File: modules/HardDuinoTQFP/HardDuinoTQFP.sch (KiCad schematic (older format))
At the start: 6 parts, among them J1 Conn_01x10_Male, J2 Conn_01x10_Male

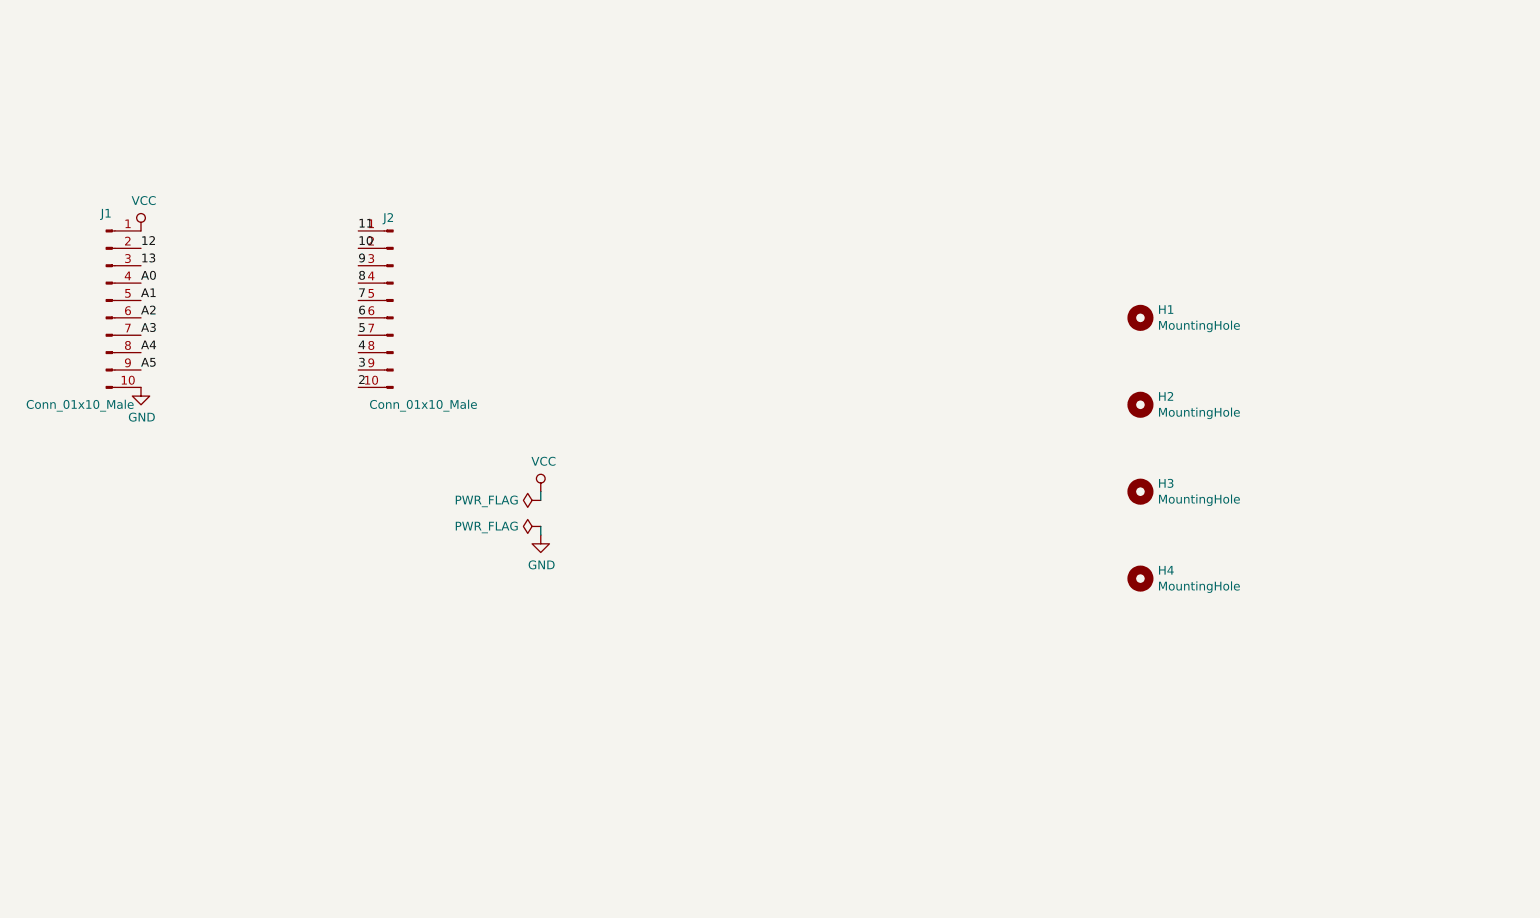
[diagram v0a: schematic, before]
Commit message: HardDuino TQFP is ready
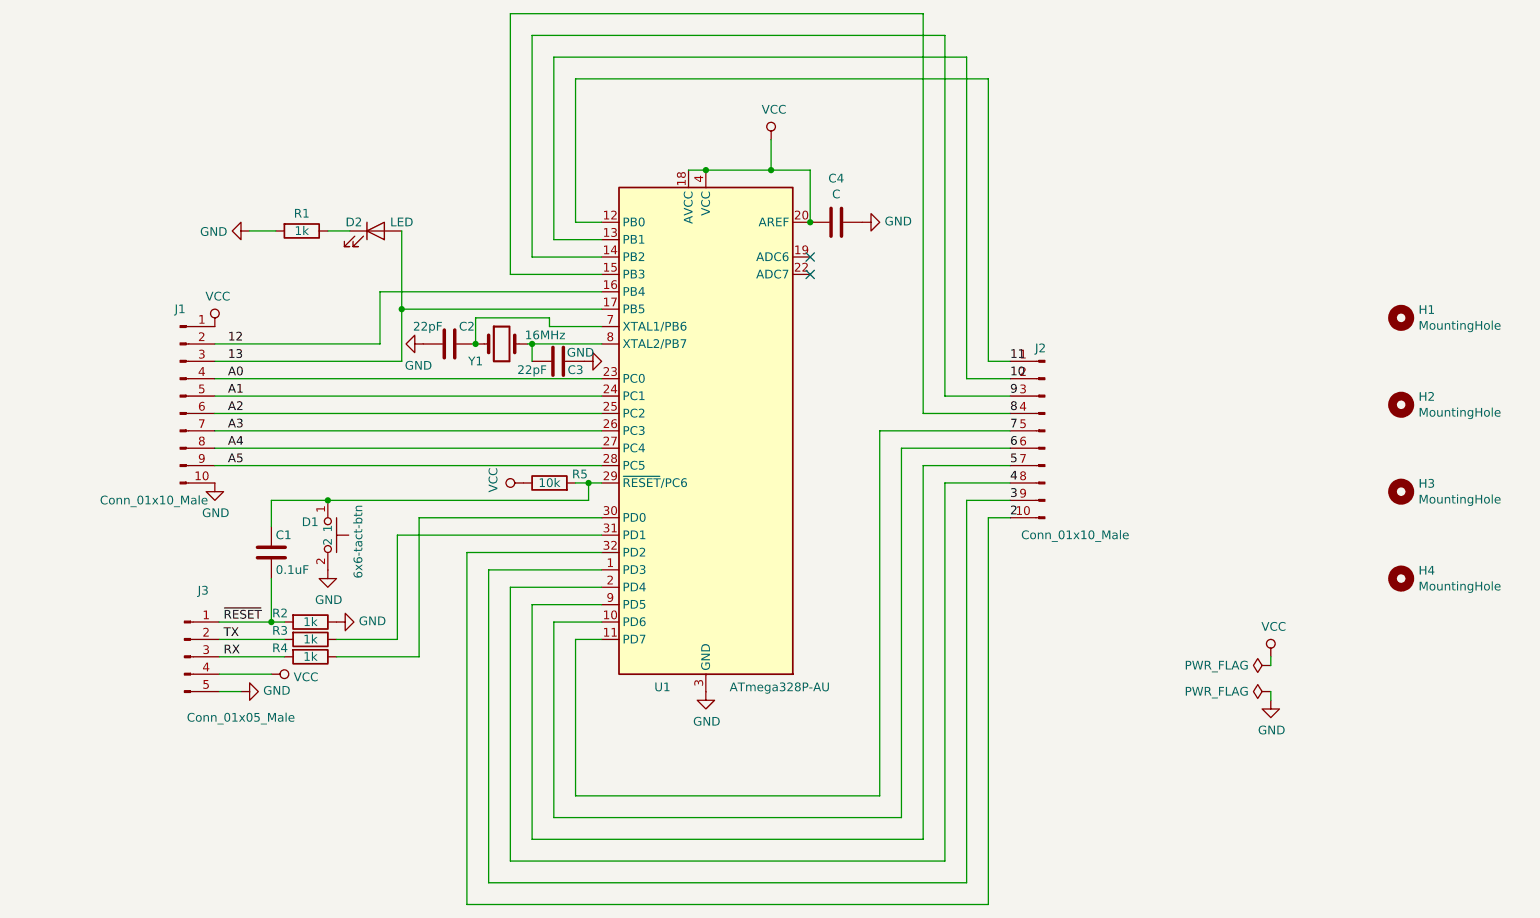
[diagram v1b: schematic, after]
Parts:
- added C1: 0.1uF, Capacitor_SMD:C_0805_2012Metric_Pad1.15x1.40mm_HandSolder, symbol Device:C
- added C2, C3: 22pF, Capacitor_SMD:C_0805_2012Metric_Pad1.15x1.40mm_HandSolder, symbol Device:C
- added C4: C, Capacitor_SMD:C_0805_2012Metric_Pad1.15x1.40mm_HandSolder, symbol Device:C
- added D1: 6x6-tact-btn, CommonLibrary:6x6-tact-btn, symbol CommonLibrary:6x6-tact-btn
- added D2: LED, LED_SMD:LED_0805_2012Metric_Pad1.15x1.40mm_HandSolder, symbol Device:LED
- added J3: Conn_01x05_Male, Connector_PinHeader_2.54mm:PinHeader_1x05_P2.54mm_Vertical, symbol Connector:Conn_01x05_Male
- added R1, R2, R3, R4: 1k, Resistor_SMD:R_0805_2012Metric_Pad1.15x1.40mm_HandSolder, symbol Device:R
- added R5: 10k, Resistor_SMD:R_0805_2012Metric_Pad1.15x1.40mm_HandSolder, symbol Device:R
- added U1: ATmega328P-AU, Package_QFP:TQFP-32_7x7mm_P0.8mm, symbol MCU_Microchip_ATmega:ATmega328P-AU
- added Y1: 16MHz, Crystal:Crystal_HC49-U_Vertical, symbol Device:Crystal
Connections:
- net 10: now also U1.13 (PB1)
- net 11: now also U1.12 (PB0)
- net 12: now also U1.16 (PB4)
- net 13: now also D2.2 (A), U1.17 (PB5)
- net 2: now also U1.32 (PD2)
- net 3: now also U1.1 (PD3)
- net 4: now also U1.2 (PD4)
- net 5: now also U1.9 (PD5)
- net 6: now also U1.10 (PD6)
- net 7: now also U1.11 (PD7)
- net 8: now also U1.15 (PB3)
- net 9: now also U1.14 (PB2)
- net A0: now also U1.23 (PC0)
- net A1: now also U1.24 (PC1)
- net A2: now also U1.25 (PC2)
- net A3: now also U1.26 (PC3)
- net A4: now also U1.27 (PC4)
- net A5: now also U1.28 (PC5)
- net GND: now also C2.2, C3.1, C4.1, D1.2, J3.5 (Pin_5), R1.2, R2.1, U1.21 (GND), U1.3 (GND), U1.5 (GND)
- net VCC: now also C4.2, J3.4 (Pin_4), R5.1, U1.18 (AVCC), U1.20 (AREF), U1.4 (VCC), U1.6 (VCC)
- new net: C1.1, D1.1, R5.2, U1.29 (~RESET~/PC6)
- new net: R4.1, U1.30 (PD0)
- new net: R3.1, U1.31 (PD1)
- new net: C2.1, U1.7 (XTAL1/PB6), Y1.1
- new net: C3.2, U1.8 (XTAL2/PB7), Y1.2
- new net: D2.1 (K), R1.1
- new net RX: J3.3 (Pin_3), R4.2
- new net TX: J3.2 (Pin_2), R3.2
- new net ~RESET: C1.2, J3.1 (Pin_1), R2.2
- no-connect marks 0 -> 2
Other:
- moved on the sheet: H1, H2, H3, H4, J1, J2

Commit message: HardDuinoTQFP: fix pin numbering (8 and 12 was mixed up) Add ISP pinheader
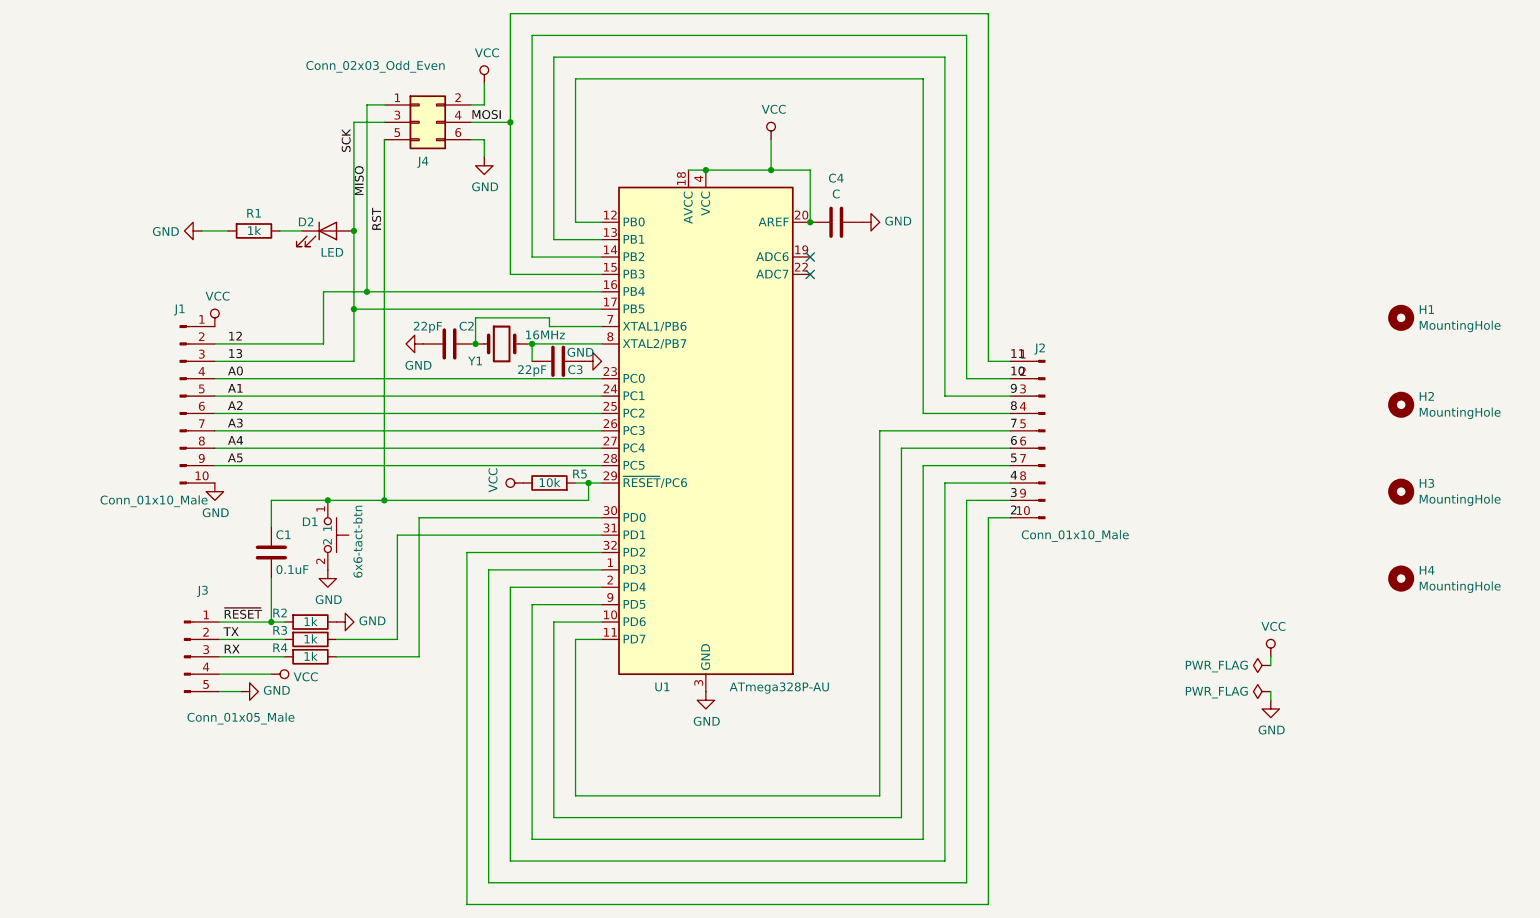
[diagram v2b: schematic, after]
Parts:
- added J4: Conn_02x03_Odd_Even, Connector_PinHeader_2.54mm:PinHeader_2x03_P2.54mm_Vertical, symbol Connector_Generic:Conn_02x03_Odd_Even
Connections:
- net 10: now also U1.14 (PB2); no longer U1.13 (PB1)
- net 11: now also U1.15 (PB3), J4.4 (Pin_4); no longer U1.12 (PB0)
- net 12: now also J4.1 (Pin_1)
- net 13: now also J4.3 (Pin_3)
- net 8: now also U1.12 (PB0); no longer U1.15 (PB3)
- net 9: now also U1.13 (PB1); no longer U1.14 (PB2)
- net GND: now also J4.6 (Pin_6)
- net VCC: now also J4.2 (Pin_2)
- net RST: now reaches C1.1, D1.1, R5.2, U1.29 (~RESET~/PC6)
- net RST: now also J4.5 (Pin_5)
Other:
- moved on the sheet: D2, R1
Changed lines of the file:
@@
 	4250 1950 4250 1125
 Wire Wire Line
-	4250 1125 6625 1125
-Wire Wire Line
-	6625 1125 6625 2750
-Wire Wire Line
 	6625 3650 6625 5875
 Wire Wire Line
@@
 	4125 2050 4125 1000
 Wire Wire Line
-	4125 1000 6500 1000
-Wire Wire Line
-	6500 1000 6500 2850
-Wire Wire Line
 	6500 2850 6750 2850
 Wire Wire Line
@@
 	4000 2150 4000 875
 Wire Wire Line
-	4000 875  6375 875
-Wire Wire Line
-	6375 875  6375 2950
-Wire Wire Line
 	6375 2950 6750 2950
 Wire Wire Line
 	4400 2250 3875 2250
 Wire Wire Line
-	3875 2250 3875 750
-Wire Wire Line
-	3875 750  6250 750
-Wire Wire Line
-	6250 750  6250 3050
-Wire Wire Line
 	6250 3050 6750 3050
 Wire Wire Line
-	3250 2450 4400 2450
-Wire Wire Line
-	3125 2350 4400 2350
-Wire Wire Line
 	2175 2850 4400 2850
 Wire Wire Line
-	2175 2750 3250 2750
-Wire Wire Line
-	2175 2650 3125 2650
-Wire Wire Line
-	3125 2350 3125 2650
+	2175 2750 2975 2750
+Wire Wire Line
+	2175 2650 2800 2650
 Wire Wire Line
 	4400 2950 2175 2950
@@
 L Device:LED D2
 U 1 1 5EC11726
-P 3100 2000
-F 0 "D2" H 2975 2050 50  0000 C CNN
-F 1 "LED" H 3250 2050 50  0000 C CNN
-F 2 "LED_SMD:LED_0805_2012Metric_Pad1.15x1.40mm_HandSolder" H 3100 2000 50  0001 C CNN
-F 3 "~" H 3100 2000 50  0001 C CNN
-	1    3100 2000
+P 2825 2000
+F 0 "D2" H 2700 2050 50  0000 C CNN
+F 1 "LED" H 2850 1875 50  0000 C CNN
+F 2 "LED_SMD:LED_0805_2012Metric_Pad1.15x1.40mm_HandSolder" H 2825 2000 50  0001 C CNN
+F 3 "~" H 2825 2000 50  0001 C CNN
+	1    2825 2000
 	1    0    0    -1
 $EndComp
@@
 L Device:R R1
 U 1 1 5EC11FBF
-P 2675 2000
-F 0 "R1" V 2575 2000 50  0000 C CNN
-F 1 "1k" V 2675 2000 50  0000 C CNN
-F 2 "Resistor_SMD:R_0805_2012Metric_Pad1.15x1.40mm_HandSolder" V 2605 2000 50  0001 C CNN
-F 3 "~" H 2675 2000 50  0001 C CNN
-	1    2675 2000
+P 2400 2000
+F 0 "R1" V 2300 2000 50  0000 C CNN
+F 1 "1k" V 2400 2000 50  0000 C CNN
+F 2 "Resistor_SMD:R_0805_2012Metric_Pad1.15x1.40mm_HandSolder" V 2330 2000 50  0001 C CNN
+F 3 "~" H 2400 2000 50  0001 C CNN
+	1    2400 2000
 	0    1    1    0
 $EndComp
@@
 L power:GND #PWR02
 U 1 1 5EC15A85
-P 2375 2000
-F 0 "#PWR02" H 2375 1750 50  0001 C CNN
-F 1 "GND" V 2380 1872 50  0000 R CNN
-F 2 "" H 2375 2000 50  0001 C CNN
-F 3 "" H 2375 2000 50  0001 C CNN
-	1    2375 2000
-	0    1    1    0
-$EndComp
-Wire Wire Line
-	2375 2000 2525 2000
-Wire Wire Line
-	2825 2000 2950 2000
-Wire Wire Line
-	3250 2000 3250 2450
-Connection ~ 3250 2450
+P 2100 2000
+F 0 "#PWR02" H 2100 1750 50  0001 C CNN
+F 1 "GND" V 2105 1872 50  0000 R CNN
+F 2 "" H 2100 2000 50  0001 C CNN
+F 3 "" H 2100 2000 50  0001 C CNN
+	1    2100 2000
+	0    1    1    0
+$EndComp
+Wire Wire Line
+	2100 2000 2250 2000
+Wire Wire Line
+	2550 2000 2675 2000
 $Comp
 L Device:Crystal Y1
@@
 $EndComp
 Connection ~ 3675 2650
-Wire Wire Line
-	3250 2450 3250 2750
 $Comp
 L power:GND #PWR06
@@
 Connection ~ 2825 3550
 Wire Wire Line
-	2825 3550 4325 3550
+	2825 3550 3150 3550
 $Comp
 L power:VCC #PWR010
@@
 NoConn ~ 5600 2150
 NoConn ~ 5600 2250
+Wire Wire Line
+	4250 1125 6250 1125
+Wire Wire Line
+	6250 1125 6250 3050
+Wire Wire Line
+	4125 1000 6375 1000
+Wire Wire Line
+	6375 1000 6375 2950
+Wire Wire Line
+	4000 875  6500 875
+Wire Wire Line
+	6500 875  6500 2850
+Wire Wire Line
+	3875 750  6625 750
+Wire Wire Line
+	6625 750  6625 2750
+Wire Wire Line
+	2800 2350 2800 2650
+Wire Wire Line
+	2800 2350 3050 2350
+Wire Wire Line
+	2975 2000 2975 2450
+Wire Wire Line
+	2975 2450 4400 2450
+Connection ~ 2975 2450
+Wire Wire Line
+	2975 2450 2975 2750
+$Comp
+L Connector_Generic:Conn_02x03_Odd_Even J4
+U 1 1 5ED4B353
+P 3350 1375
+F 0 "J4" H 3375 1150 50  0000 C CNN
+F 1 "Conn_02x03_Odd_Even" H 3100 1700 50  0000 C CNN
+F 2 "Connector_PinHeader_2.54mm:PinHeader_2x03_P2.54mm_Vertical" H 3350 1375 50  0001 C CNN
+F 3 "~" H 3350 1375 50  0001 C CNN
+	1    3350 1375
+	1    0    0    -1
+$EndComp
+$Comp
+L power:GND #PWR013
+U 1 1 5ED5004C
+P 3725 1575
+F 0 "#PWR013" H 3725 1325 50  0001 C CNN
+F 1 "GND" H 3730 1402 50  0000 C CNN
+F 2 "" H 3725 1575 50  0001 C CNN
+F 3 "" H 3725 1575 50  0001 C CNN
+	1    3725 1575
+	1    0    0    -1
+$EndComp
+Wire Wire Line
+	3650 1475 3725 1475
+Wire Wire Line
+	3725 1475 3725 1575
+$Comp
+L power:VCC #PWR012
+U 1 1 5ED541F1
+P 3725 1150
+F 0 "#PWR012" H 3725 1000 50  0001 C CNN
+F 1 "VCC" H 3742 1323 50  0000 C CNN
+F 2 "" H 3725 1150 50  0001 C CNN
+F 3 "" H 3725 1150 50  0001 C CNN
+	1    3725 1150
+	1    0    0    -1
+$EndComp
+Wire Wire Line
+	3650 1275 3725 1275
+Wire Wire Line
+	3725 1275 3725 1150
+Wire Wire Line
+	3875 750  3875 1375
+Wire Wire Line
+	3650 1375 3875 1375
+Connection ~ 3875 1375
+Wire Wire Line
+	3875 1375 3875 2250
+Wire Wire Line
+	2975 2000 2975 1375
+Wire Wire Line
+	2975 1375 3150 1375
+Connection ~ 2975 2000
+Wire Wire Line
+	3050 1275 3050 2350
+Connection ~ 3050 2350
+Wire Wire Line
+	3050 1275 3150 1275
+Wire Wire Line
+	3050 2350 4400 2350
+Wire Wire Line
+	3150 1475 3150 3550
+Connection ~ 3150 3550
+Wire Wire Line
+	3150 3550 4325 3550
+Text Label 3650 1375 0    50   ~ 0
+MOSI
+Text Label 3050 1800 1    50   ~ 0
+MISO
+Text Label 2975 1550 1    50   ~ 0
+SCK
+Text Label 3150 2000 1    50   ~ 0
+RST
 $EndSCHEMATC

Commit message: HardDuinoTQFP. Add photomask & hash
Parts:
- added J5: Conn_01x01_Male, Connector_PinHeader_2.54mm:PinHeader_1x01_P2.54mm_Vertical, symbol Connector:Conn_01x01_Male
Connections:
- net at C2.1, U1.7 (XTAL1/PB6), Y1.1: now also J5.1 (Pin_1)
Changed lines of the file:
@@
 Text Label 3150 2000 1    50   ~ 0
 RST
+$Comp
+L Connector:Conn_01x01_Male J5
+U 1 1 5ED32770
+P 3475 2250
+F 0 "J5" H 3583 2431 50  0000 C CNN
+F 1 "Conn_01x01_Male" H 3583 2340 50  0000 C CNN
+F 2 "Connector_PinHeader_2.54mm:PinHeader_1x01_P2.54mm_Vertical" H 3475 2250 50  0001 C CNN
+F 3 "~" H 3475 2250 50  0001 C CNN
+	1    3475 2250
+	1    0    0    -1
+$EndComp
+Wire Wire Line
+	3675 2250 3675 2500
+Connection ~ 3675 2500
 $EndSCHEMATC
